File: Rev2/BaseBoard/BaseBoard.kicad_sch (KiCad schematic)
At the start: 12 parts, among them J7 AVR-JTAG-10, SW1 SW_Push, U3 ESP32-WROOM-32E, Y1 Crystal

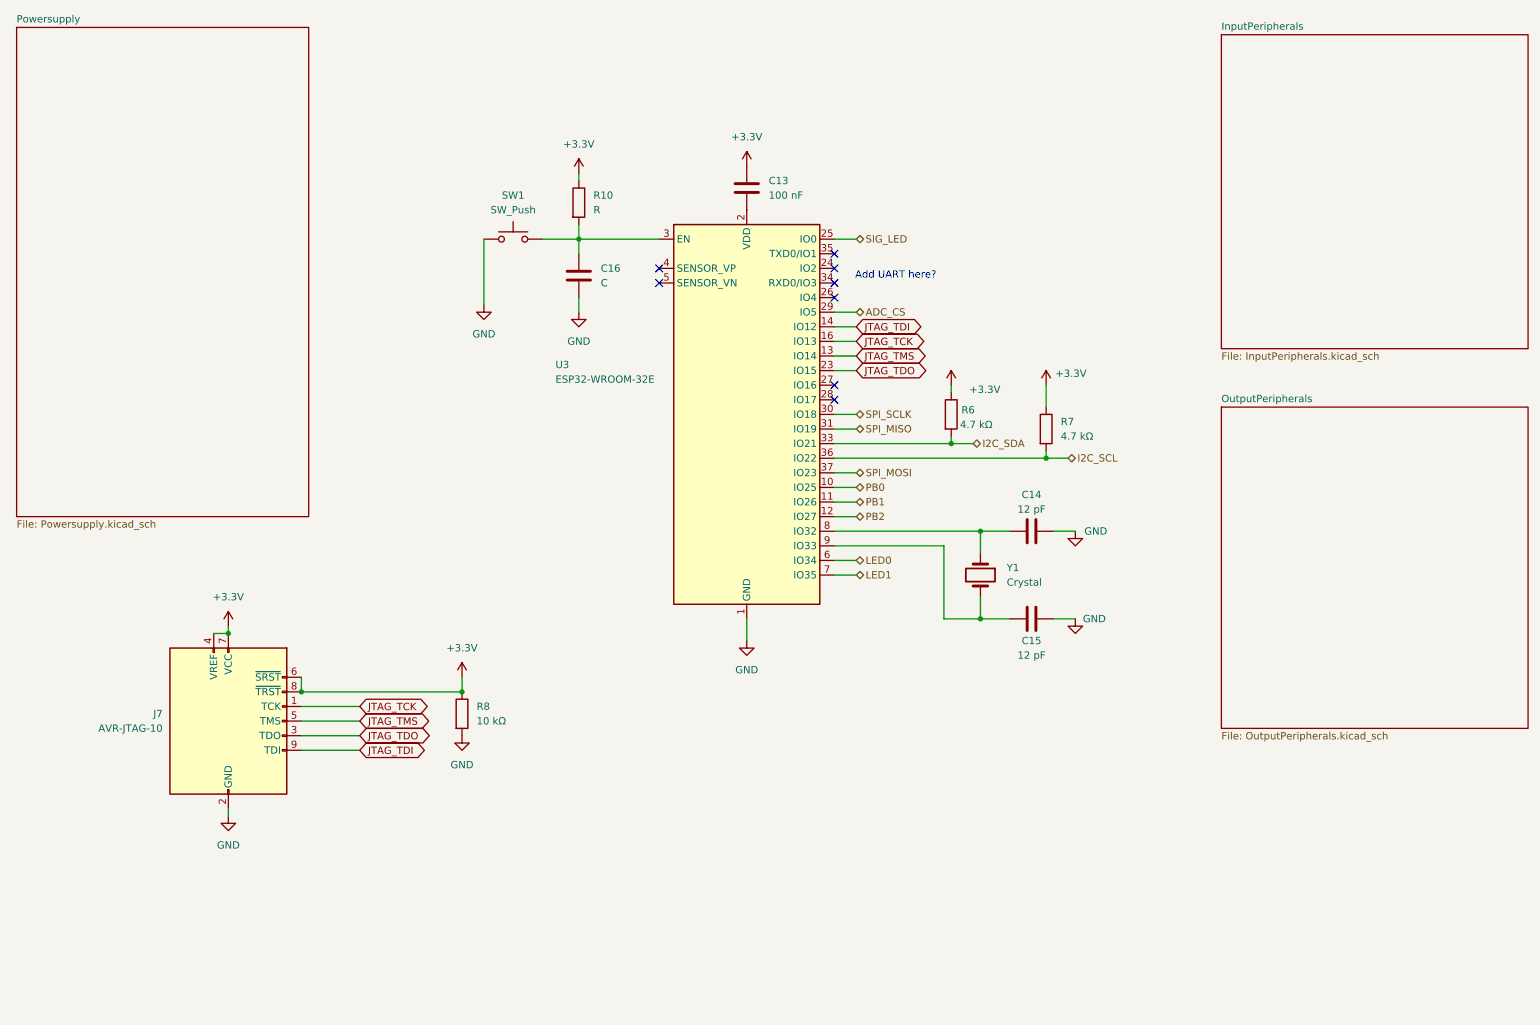
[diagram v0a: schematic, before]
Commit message: Added Testpoints, UART and JTAG
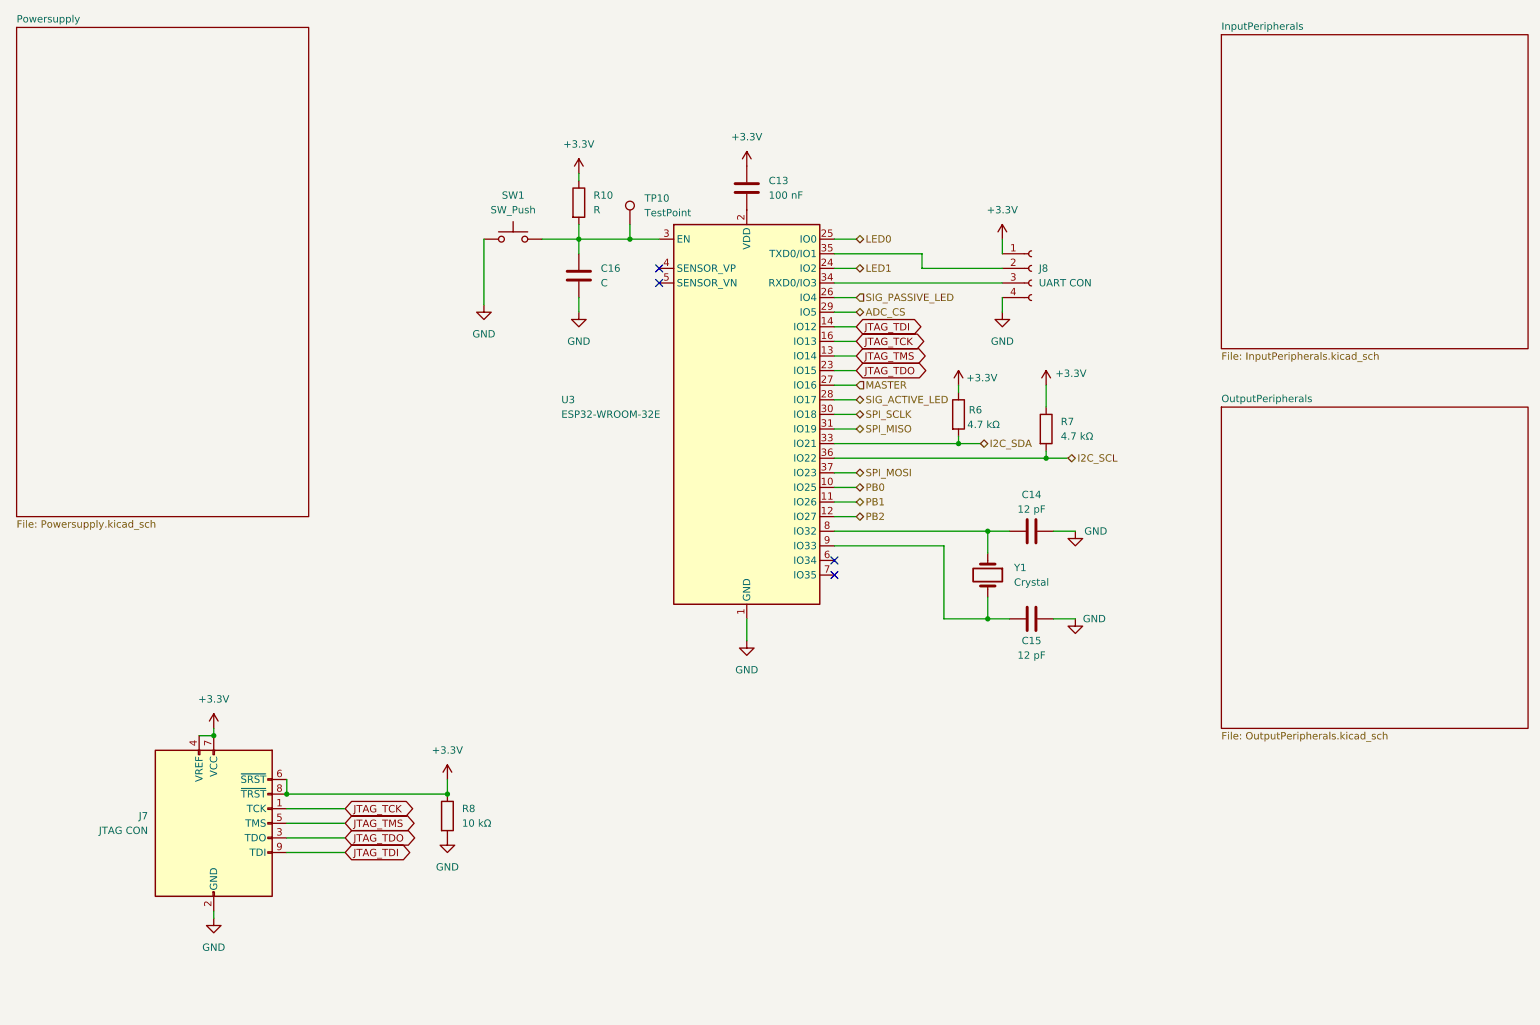
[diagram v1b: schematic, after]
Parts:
- added J8: UART CON, symbol Connector:Conn_01x04_Socket
- added TP10: TestPoint, symbol Connector:TestPoint
- J7: value AVR-JTAG-10 -> JTAG CON
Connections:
- net SIG_LED is gone; now on net LED0: U3.25 (IO0)
- net +3.3V: now also J8.1 (Pin_1)
- net GND: now also J8.4 (Pin_4)
- net LED0: no longer U3.6 (IO34)
- net LED1: now also U3.24 (IO2); no longer U3.7 (IO35)
- net at C16.1, R10.2, SW1.2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: now also TP10.1
- net SIG_PASSIVE_LED: now reaches U3.26 (IO4)
- net MASTER: now reaches U3.27 (IO16)
- net SIG_ACTIVE_LED: now reaches U3.28 (IO17)
- net at U3.34 (RXD0/IO3): now also J8.3 (Pin_3)
- net at U3.35 (TXD0/IO1): now also J8.2 (Pin_2)
- no-connect marks 8 -> 4
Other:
- note removed: "Add UART here?"
- moved on the sheet: J7, R6, R8, Y1

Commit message: Finished placement, routing remains
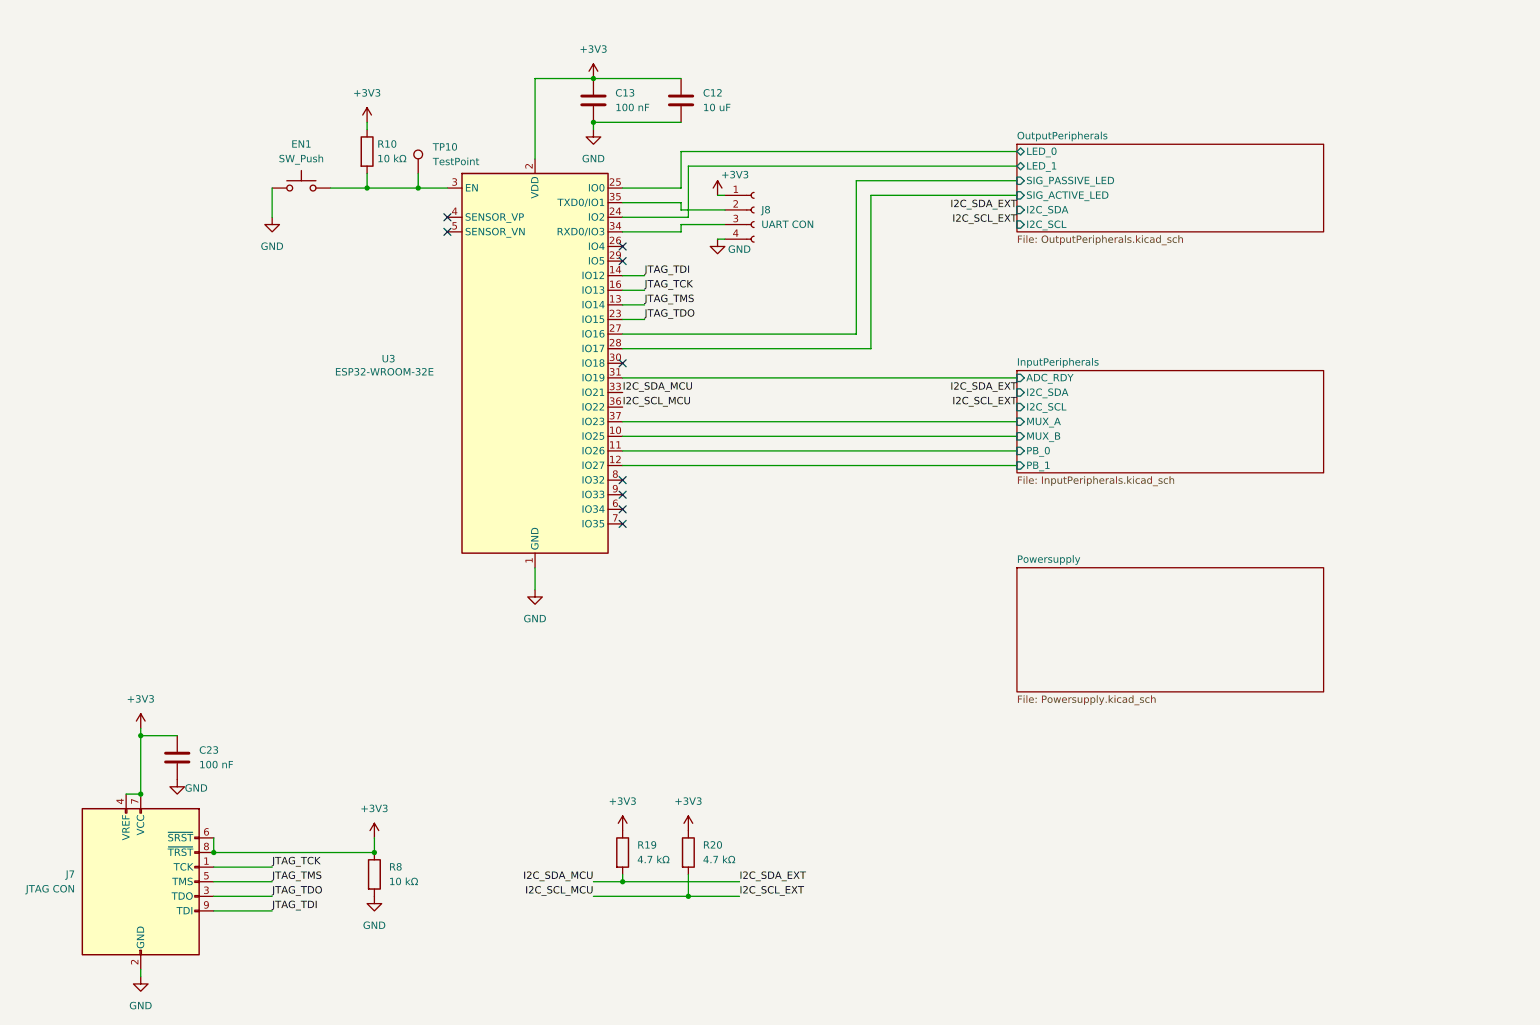
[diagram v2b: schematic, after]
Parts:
- removed C14, C15: 12 pF, symbol Device:C
- removed C16: C, symbol Device:C
- removed R6, R7: 4.7 kΩ, symbol Device:R
- removed Y1: Crystal, symbol Device:Crystal
- added C12: 10 uF, Capacitor_SMD:C_0805_2012Metric_Pad1.18x1.45mm_HandSolder, symbol Device:C
- added C23: 100 nF, Capacitor_SMD:C_0805_2012Metric_Pad1.18x1.45mm_HandSolder, symbol Device:C
- added R19, R20: 4.7 kΩ, Resistor_SMD:R_0805_2012Metric_Pad1.20x1.40mm_HandSolder, symbol Device:R
- C13: footprint (none) -> Capacitor_SMD:C_0805_2012Metric_Pad1.18x1.45mm_HandSolder
- EN1: renamed from SW1; footprint (none) -> Button_Switch_SMD:SW_Push_1P1T_NO_6x6mm_H9.5mm
- J7: footprint Connector_IDC:IDC-Header_2x05_P2.54mm_Latch6.5mm_Vertical -> Connector_IDC:IDC-Header_2x05_P2.54mm_Horizontal
- J8: footprint (none) -> Connector_PinSocket_2.54mm:PinSocket_1x04_P2.54mm_Horizontal
- R10: value R -> 10 kΩ; footprint (none) -> Resistor_SMD:R_0805_2012Metric_Pad1.20x1.40mm_HandSolder
- R8: footprint (none) -> Resistor_SMD:R_0805_2012Metric_Pad1.20x1.40mm_HandSolder
- TP10: footprint (none) -> TestPoint:TestPoint_Pad_1.0x1.0mm
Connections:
- net +3.3V is gone; now on net +3V3: C13.1, J7.4 (VREF), J7.6 (~{SRST}), J7.7 (VCC), J7.8 (~{TRST}), J8.1 (Pin_1), R10.1, R8.1
- net GND: now also C13.2, C12.2, C23.2
- net +3V3: now reaches U3.2 (VDD)
- net +3V3: now also C12.1, C23.1, R19.1, R20.1; no longer C13.2
- net ADC_CS: no longer names the net of U3.29 (IO5)
- net I2C_SCL renamed I2C_SCL_EXT
- net I2C_SCL_EXT: now also R20.2
- net I2C_SDA renamed I2C_SDA_EXT
- net I2C_SDA_EXT: now also R19.2
- net LED0 renamed OutputPeripherals/LED_0
- net LED1 renamed OutputPeripherals/LED_1
- net MASTER renamed OutputPeripherals/SIG_PASSIVE_LED
- net PB0 renamed InputPeripherals/MUX_B
- net PB1 renamed InputPeripherals/PB_0
- net PB2 renamed InputPeripherals/PB_1
- net SIG_ACTIVE_LED renamed OutputPeripherals/SIG_ACTIVE_LED
- net SIG_PASSIVE_LED: no longer names the net of U3.26 (IO4)
- net SPI_MISO renamed InputPeripherals/ADC_RDY
- net SPI_MOSI renamed InputPeripherals/MUX_A
- net SPI_SCLK: no longer names the net of U3.30 (IO18)
- no-connect marks 4 -> 9
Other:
- sheet InputPeripherals ports: added ADC_RDY, I2C_SCL, I2C_SDA, MUX_A, MUX_B, PB_0, PB_1; removed none
- sheet OutputPeripherals ports: added I2C_SCL, I2C_SDA, LED_0, LED_1, SIG_ACTIVE_LED, SIG_PASSIVE_LED; removed none
- moved on the sheet: C13, EN1, J7, J8, R10, R8, TP10, U3
